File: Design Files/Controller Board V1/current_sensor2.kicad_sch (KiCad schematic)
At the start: 5 parts, among them U3 INA219BIDR

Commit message: resistor footprints
yuh
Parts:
- R1: renamed from R5; footprint (none) -> Resistor_SMD:R_0805_2012Metric
- R2: renamed from R6; footprint (none) -> Resistor_SMD:R_0603_1608Metric
- R3: renamed from R7; footprint (none) -> Resistor_SMD:R_0603_1608Metric
- R4: renamed from R8; footprint (none) -> Resistor_SMD:R_0603_1608Metric
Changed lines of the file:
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@@
 		(on_board yes)
 		(dnp no)
-		(property "Reference" "R7"
+		(property "Reference" "R3"
 			(at 160.02 98.044 0)
 			(effects
@@
 			)
 		)
-		(property "Footprint" ""
+		(property "Footprint" "Resistor_SMD:R_0603_1608Metric"
 			(at 159.512 99.06 90)
 			(effects
@@
 			(project "Control Board V1"
 				(path "/e0c606b8-cbb9-4aff-b96c-73876da6ca74/baf458a5-80d6-4ce7-aba0-1e3ff07021ab"
-					(reference "R7")
+					(reference "R3")
 					(unit 1)
 				)
@@
 		(dnp no)
 		(fields_autoplaced yes)
-		(property "Reference" "R5"
+		(property "Reference" "R1"
 			(at 135.89 86.36 90)
 			(effects
@@
 			)
 		)
-		(property "Footprint" ""
+		(property "Footprint" "Resistor_SMD:R_0805_2012Metric"
 			(at 135.89 94.488 90)
 			(effects
@@
 			(project "Control Board V1"
 				(path "/e0c606b8-cbb9-4aff-b96c-73876da6ca74/baf458a5-80d6-4ce7-aba0-1e3ff07021ab"
-					(reference "R5")
+					(reference "R1")
 					(unit 1)
 				)
@@
 		(on_board yes)
 		(dnp no)
-		(property "Reference" "R8"
+		(property "Reference" "R4"
 			(at 166.37 98.044 0)
 			(effects
@@
 			)
 		)
-		(property "Footprint" ""
+		(property "Footprint" "Resistor_SMD:R_0603_1608Metric"
 			(at 165.862 99.06 90)
 			(effects
@@
 			(project "Control Board V1"
 				(path "/e0c606b8-cbb9-4aff-b96c-73876da6ca74/baf458a5-80d6-4ce7-aba0-1e3ff07021ab"
-					(reference "R8")
+					(reference "R4")
 					(unit 1)
 				)
@@
 		(on_board yes)
 		(dnp no)
-		(property "Reference" "R6"
+		(property "Reference" "R2"
 			(at 153.67 98.044 0)
 			(effects
@@
 			)
 		)
-		(property "Footprint" ""
+		(property "Footprint" "Resistor_SMD:R_0603_1608Metric"
 			(at 153.162 99.06 90)
 			(effects
@@
 			(project "Control Board V1"
 				(path "/e0c606b8-cbb9-4aff-b96c-73876da6ca74/baf458a5-80d6-4ce7-aba0-1e3ff07021ab"
-					(reference "R6")
-					(unit 1)
-				)
+					(reference "R2")
+					(unit 1)
+				)

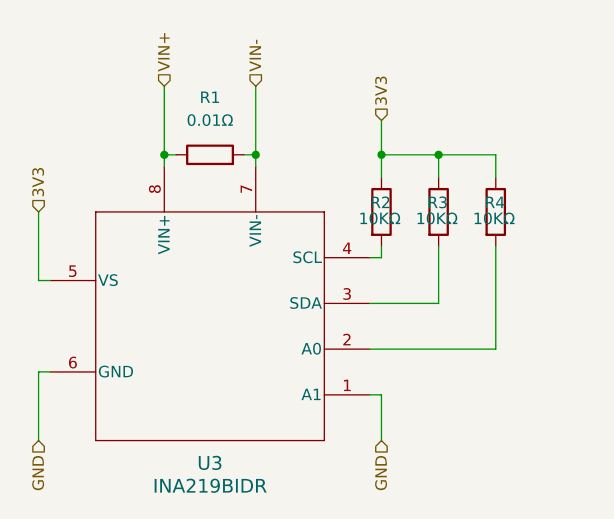
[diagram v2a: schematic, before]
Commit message: I2C channels for pico and current sensors
gaming B)
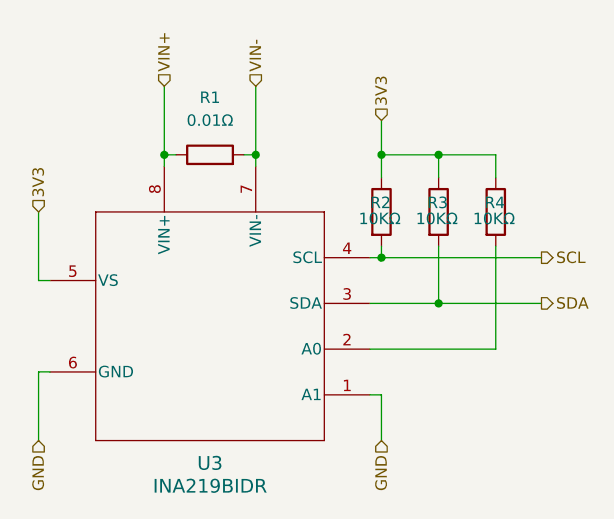
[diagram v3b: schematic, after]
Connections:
- net SDA: now reaches R3.2, U3.3 (SDA)
- net SCL: now reaches R2.2, U3.4 (SCL)
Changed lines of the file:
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@@
 	(paper "A4")
 	(junction
+		(at 161.29 109.22)
+		(diameter 0)
+		(color 0 0 0 0)
+	)
+	(junction
+		(at 154.94 104.14)
+		(diameter 0)
+		(color 0 0 0 0)
+	)
+	(junction
 		(at 161.29 92.71)
 		(diameter 0)
@@
 	(wire
 		(pts
+			(xy 154.94 104.14) (xy 172.72 104.14)
+		)
+		(stroke
+			(width 0)
+			(type default)
+		)
+	)
+	(wire
+		(pts
 			(xy 154.94 119.38) (xy 154.94 124.46)
 		)
@@
 	(wire
 		(pts
+			(xy 161.29 109.22) (xy 172.72 109.22)
+		)
+		(stroke
+			(width 0)
+			(type default)
+		)
+	)
+	(wire
+		(pts
 			(xy 167.64 92.71) (xy 167.64 95.25)
 		)
@@
 		(shape input)
 		(at 116.84 124.46 270)
+		(fields_autoplaced yes)
 		(effects
 			(font
@@
 		(shape input)
 		(at 154.94 88.9 90)
+		(fields_autoplaced yes)
 		(effects
 			(font
@@
 		(shape input)
 		(at 116.84 99.06 90)
+		(fields_autoplaced yes)
+		(effects
+			(font
+				(size 1.27 1.27)
+			)
+			(justify left)
+		)
+	)
+	(hierarchical_label "SCL"
+		(shape output)
+		(at 172.72 104.14 0)
+		(fields_autoplaced yes)
+		(effects
+			(font
+				(size 1.27 1.27)
+			)
+			(justify left)
+		)
+	)
+	(hierarchical_label "SDA"
+		(shape output)
+		(at 172.72 109.22 0)
+		(fields_autoplaced yes)
 		(effects
 			(font
@@
 		(shape input)
 		(at 140.97 85.09 90)
+		(fields_autoplaced yes)
 		(effects
 			(font
@@
 		(shape input)
 		(at 154.94 124.46 270)
+		(fields_autoplaced yes)
 		(effects
 			(font
@@
 		(shape input)
 		(at 130.81 85.09 90)
-		(effects
-			(font
+		(fields_autoplaced yes)
+		(effects
+			(font

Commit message: Assigning footprints and ading to schematic
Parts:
- renumbered R1 to R5, R2 to R6, R3 to R7, R4 to R8
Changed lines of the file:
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@@
 		(shape input)
 		(at 116.84 124.46 270)
-		(fields_autoplaced yes)
 		(effects
 			(font
@@
 		(shape input)
 		(at 154.94 88.9 90)
-		(fields_autoplaced yes)
 		(effects
 			(font
@@
 		(shape input)
 		(at 116.84 99.06 90)
-		(fields_autoplaced yes)
 		(effects
 			(font
@@
 		(shape output)
 		(at 172.72 104.14 0)
-		(fields_autoplaced yes)
 		(effects
 			(font
@@
 		(shape output)
 		(at 172.72 109.22 0)
-		(fields_autoplaced yes)
 		(effects
 			(font
@@
 		(shape input)
 		(at 140.97 85.09 90)
-		(fields_autoplaced yes)
 		(effects
 			(font
@@
 		(shape input)
 		(at 154.94 124.46 270)
-		(fields_autoplaced yes)
 		(effects
 			(font
@@
 		(shape input)
 		(at 130.81 85.09 90)
-		(fields_autoplaced yes)
 		(effects
 			(font
@@
 		(on_board yes)
 		(dnp no)
-		(property "Reference" "R3"
+		(property "Reference" "R7"
 			(at 160.02 98.044 0)
 			(effects
@@
 			(project "Control Board V1"
 				(path "/e0c606b8-cbb9-4aff-b96c-73876da6ca74/baf458a5-80d6-4ce7-aba0-1e3ff07021ab"
-					(reference "R3")
+					(reference "R7")
 					(unit 1)
 				)
@@
 		(dnp no)
 		(fields_autoplaced yes)
-		(property "Reference" "R1"
+		(property "Reference" "R5"
 			(at 135.89 86.36 90)
 			(effects
@@
 			(project "Control Board V1"
 				(path "/e0c606b8-cbb9-4aff-b96c-73876da6ca74/baf458a5-80d6-4ce7-aba0-1e3ff07021ab"
-					(reference "R1")
+					(reference "R5")
 					(unit 1)
 				)
@@
 		(on_board yes)
 		(dnp no)
-		(property "Reference" "R4"
+		(property "Reference" "R8"
 			(at 166.37 98.044 0)
 			(effects
@@
 			(project "Control Board V1"
 				(path "/e0c606b8-cbb9-4aff-b96c-73876da6ca74/baf458a5-80d6-4ce7-aba0-1e3ff07021ab"
-					(reference "R4")
+					(reference "R8")
 					(unit 1)
 				)
@@
 		(on_board yes)
 		(dnp no)
-		(property "Reference" "R2"
+		(property "Reference" "R6"
 			(at 153.67 98.044 0)
 			(effects
@@
 			(project "Control Board V1"
 				(path "/e0c606b8-cbb9-4aff-b96c-73876da6ca74/baf458a5-80d6-4ce7-aba0-1e3ff07021ab"
-					(reference "R2")
+					(reference "R6")
 					(unit 1)
 				)

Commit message: here we go agane
Updating footprints and tackling general layout
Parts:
- added C5: 100 nF, Capacitor_SMD:C_0603_1608Metric, symbol Device:C
- U3: footprint D0008A_N -> Library:INA219
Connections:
- net 3V3: now also C5.1
- net GND: now also C5.2
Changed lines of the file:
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@@
+	)
+	(junction
+		(at 116.84 116.84)
+		(diameter 0)
+		(color 0 0 0 0)
 	)
 	(junction
@@
 		(color 0 0 0 0)
 	)
+	(junction
+		(at 116.84 106.68)
+		(diameter 0)
+		(color 0 0 0 0)
+	)
+	(wire
+		(pts
+			(xy 153.67 109.22) (xy 161.29 109.22)
+		)
+		(stroke
+			(width 0)
+			(type default)
+		)
+	)
+	(wire
+		(pts
+			(xy 154.94 104.14) (xy 154.94 102.87)
+		)
+		(stroke
+			(width 0)
+			(type default)
+		)
+	)
+	(wire
+		(pts
+			(xy 161.29 109.22) (xy 161.29 102.87)
+		)
+		(stroke
+			(width 0)
+			(type default)
+		)
+	)
+	(wire
+		(pts
+			(xy 154.94 92.71) (xy 161.29 92.71)
+		)
+		(stroke
+			(width 0)
+			(type default)
+		)
+	)
+	(wire
+		(pts
+			(xy 139.7 92.71) (xy 140.97 92.71)
+		)
+		(stroke
+			(width 0)
+			(type default)
+		)
+	)
+	(wire
+		(pts
+			(xy 153.67 114.3) (xy 167.64 114.3)
+		)
+		(stroke
+			(width 0)
+			(type default)
+		)
+	)
+	(wire
+		(pts
+			(xy 167.64 114.3) (xy 167.64 102.87)
+		)
+		(stroke
+			(width 0)
+			(type default)
+		)
+	)
+	(wire
+		(pts
+			(xy 161.29 92.71) (xy 161.29 95.25)
+		)
+		(stroke
+			(width 0)
+			(type default)
+		)
+	)
+	(wire
+		(pts
+			(xy 116.84 115.57) (xy 116.84 116.84)
+		)
+		(stroke
+			(width 0)
+			(type default)
+		)
+	)
+	(wire
+		(pts
+			(xy 161.29 92.71) (xy 167.64 92.71)
+		)
+		(stroke
+			(width 0)
+			(type default)
+		)
+	)
 	(wire
 		(pts
@@
 	(wire
 		(pts
-			(xy 153.67 109.22) (xy 161.29 109.22)
-		)
-		(stroke
-			(width 0)
-			(type default)
-		)
-	)
-	(wire
-		(pts
-			(xy 154.94 104.14) (xy 154.94 102.87)
-		)
-		(stroke
-			(width 0)
-			(type default)
-		)
-	)
-	(wire
-		(pts
-			(xy 161.29 109.22) (xy 161.29 102.87)
-		)
-		(stroke
-			(width 0)
-			(type default)
-		)
-	)
-	(wire
-		(pts
-			(xy 154.94 92.71) (xy 161.29 92.71)
-		)
-		(stroke
-			(width 0)
-			(type default)
-		)
-	)
-	(wire
-		(pts
-			(xy 139.7 92.71) (xy 140.97 92.71)
-		)
-		(stroke
-			(width 0)
-			(type default)
-		)
-	)
-	(wire
-		(pts
-			(xy 153.67 114.3) (xy 167.64 114.3)
-		)
-		(stroke
-			(width 0)
-			(type default)
-		)
-	)
-	(wire
-		(pts
-			(xy 167.64 114.3) (xy 167.64 102.87)
-		)
-		(stroke
-			(width 0)
-			(type default)
-		)
-	)
-	(wire
-		(pts
-			(xy 161.29 92.71) (xy 161.29 95.25)
-		)
-		(stroke
-			(width 0)
-			(type default)
-		)
-	)
-	(wire
-		(pts
-			(xy 161.29 92.71) (xy 167.64 92.71)
-		)
-		(stroke
-			(width 0)
-			(type default)
-		)
-	)
-	(wire
-		(pts
 			(xy 116.84 116.84) (xy 116.84 124.46)
 		)
@@
 		(pts
 			(xy 153.67 119.38) (xy 154.94 119.38)
+		)
+		(stroke
+			(width 0)
+			(type default)
+		)
+	)
+	(wire
+		(pts
+			(xy 116.84 106.68) (xy 116.84 107.95)
 		)
 		(stroke
@@
 			)
 		)
-		(property "Footprint" "D0008A_N"
+		(property "Footprint" "Library:INA219"
 			(at 135.89 111.76 0)
 			(effects
@@
 					(unit 1)
 				)
+			)
+		)
+	)
+	(symbol
+		(lib_id "Device:C")
+		(at 116.84 111.76 0)
+		(unit 1)
+		(exclude_from_sim no)
+		(in_bom yes)
+		(on_board yes)
+		(dnp no)
+		(fields_autoplaced yes)
+		(property "Reference" "C5"
+			(at 120.65 110.4899 0)
+			(effects
+				(font
+					(size 1.27 1.27)
+				)
+				(justify left)
+			)
+		)
+		(property "Value" "100 nF"
+			(at 120.65 113.0299 0)
+			(effects
+				(font
+					(size 1.27 1.27)
+				)
+				(justify left)
+			)
+		)
+		(property "Footprint" "Capacitor_SMD:C_0603_1608Metric"
+			(at 117.8052 115.57 0)
+			(effects
+				(font
+					(size 1.27 1.27)
+				)
+				(hide yes)
+			)
+		)
+		(property "Datasheet" "~"
+			(at 116.84 111.76 0)
+			(effects
+				(font
+					(size 1.27 1.27)
+				)
+				(hide yes)
+			)
+		)
+		(property "Description" "Unpolarized capacitor"
+			(at 116.84 111.76 0)
+			(effects
+				(font
+					(size 1.27 1.27)
+				)
+				(hide yes)
+			)
+		)
+		(property "MANUFACTURER" ""
+			(at 116.84 111.76 0)
+			(effects
+				(font
+					(size 1.27 1.27)
+				)
+				(hide yes)
+			)
+		)
+		(property "MAXIMUM_PACKAGE_HEIGHT" ""
+			(at 116.84 111.76 0)
+			(effects
+				(font
+					(size 1.27 1.27)
+				)
+				(hide yes)
+			)
+		)
+		(property "PARTREV" ""
+			(at 116.84 111.76 0)
+			(effects
+				(font
+					(size 1.27 1.27)
+				)
+				(hide yes)
+			)
+		)
+		(property "SNAPEDA_PN" ""
+			(at 116.84 111.76 0)
+			(effects
+				(font
+					(size 1.27 1.27)
+				)
+				(hide yes)
+			)
+		)
+		(property "STANDARD" ""
+			(at 116.84 111.76 0)
+			(effects
+				(font
+					(size 1.27 1.27)
+				)
+				(hide yes)
+			)
+		)
+		(pin "1"
+		)
+		(pin "2"
+		)
+		(instances
+			(project "Control Board V1"
+				(path "/e0c606b8-cbb9-4aff-b96c-73876da6ca74/baf458a5-80d6-4ce7-aba0-1e3ff07021ab"
+					(reference "C5")
+					(unit 1)
+				)
